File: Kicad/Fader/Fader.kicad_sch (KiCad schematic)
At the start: 8 parts, among them J1 NCJ6FA-H, J2 NCJ6FA-H, SW1 SW_DPDT_x2, SW2 SW_DPDT_x2, SW3 SW_DPST_x2, SW4 SW_DPST_x2, SW5 SW_DPDT_x2, SW6 SW_DPDT_x2

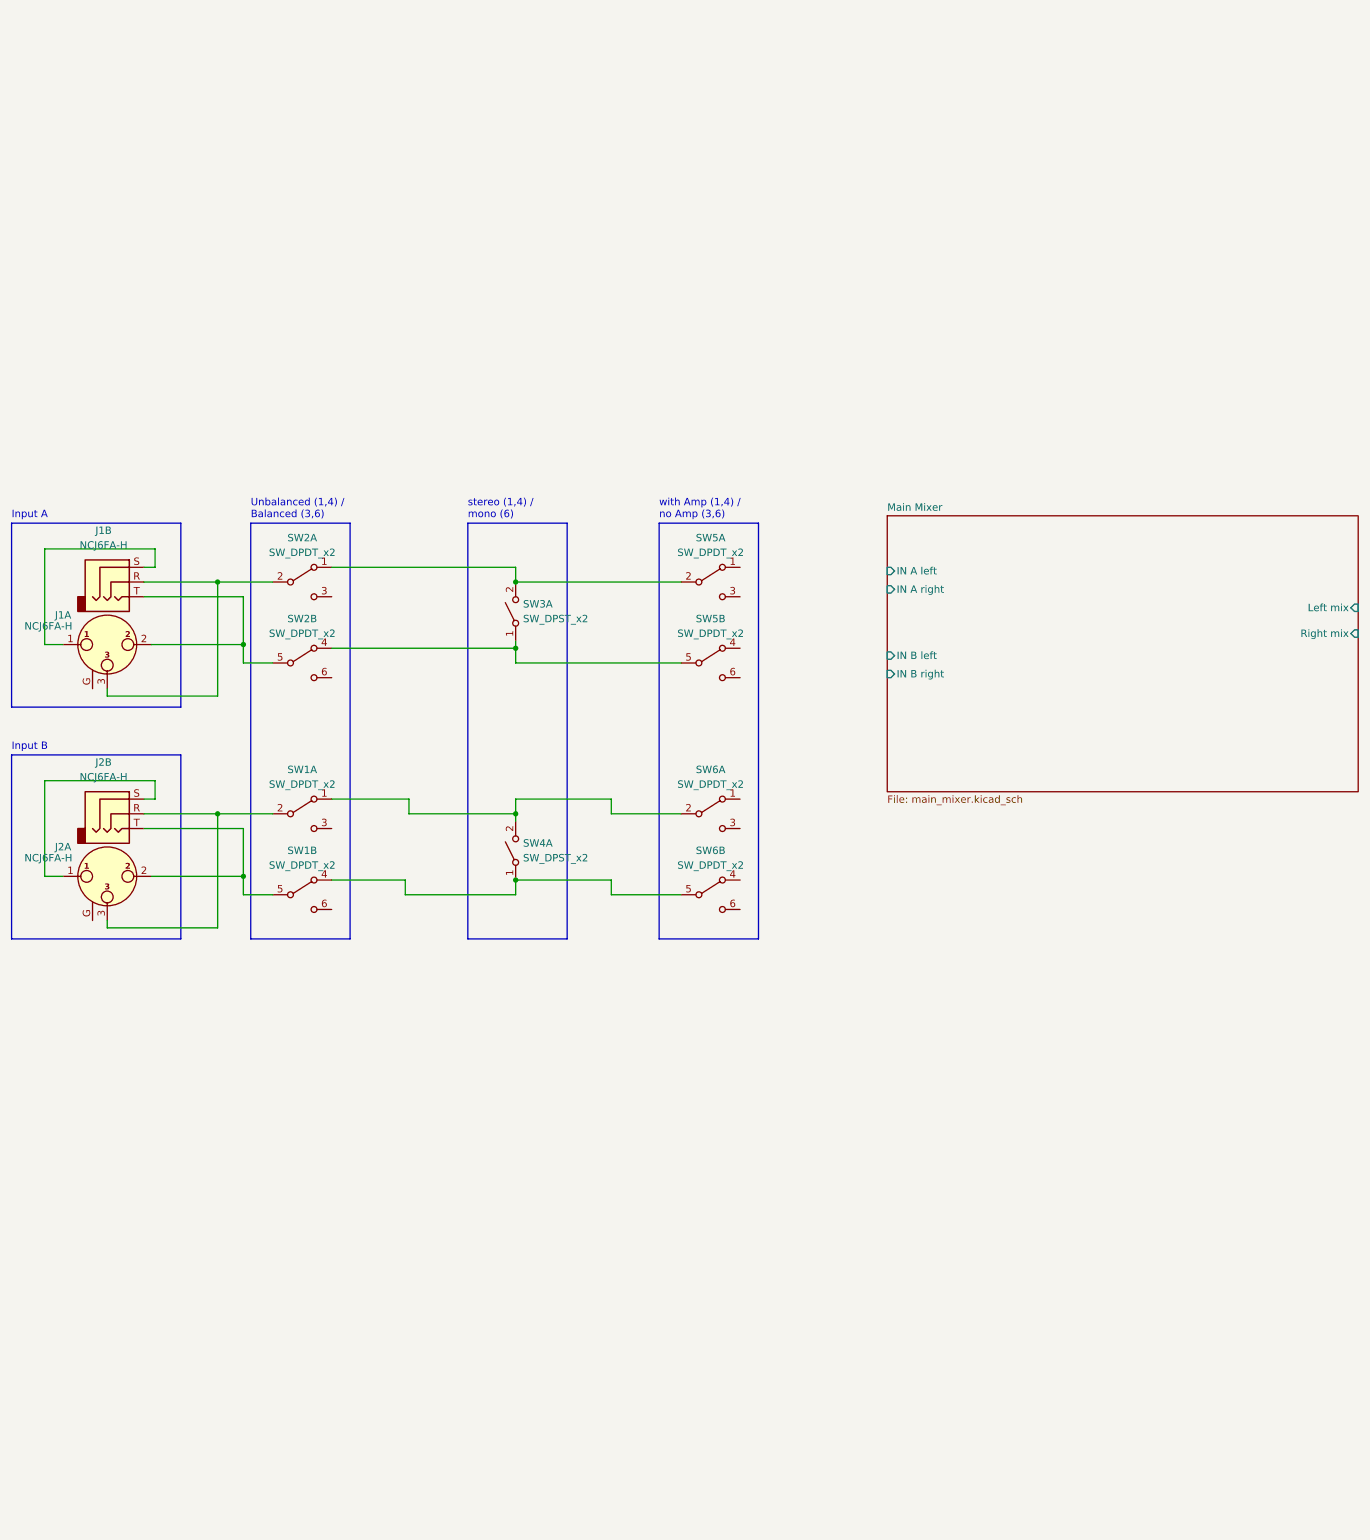
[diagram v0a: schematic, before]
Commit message: added amp and power bypass
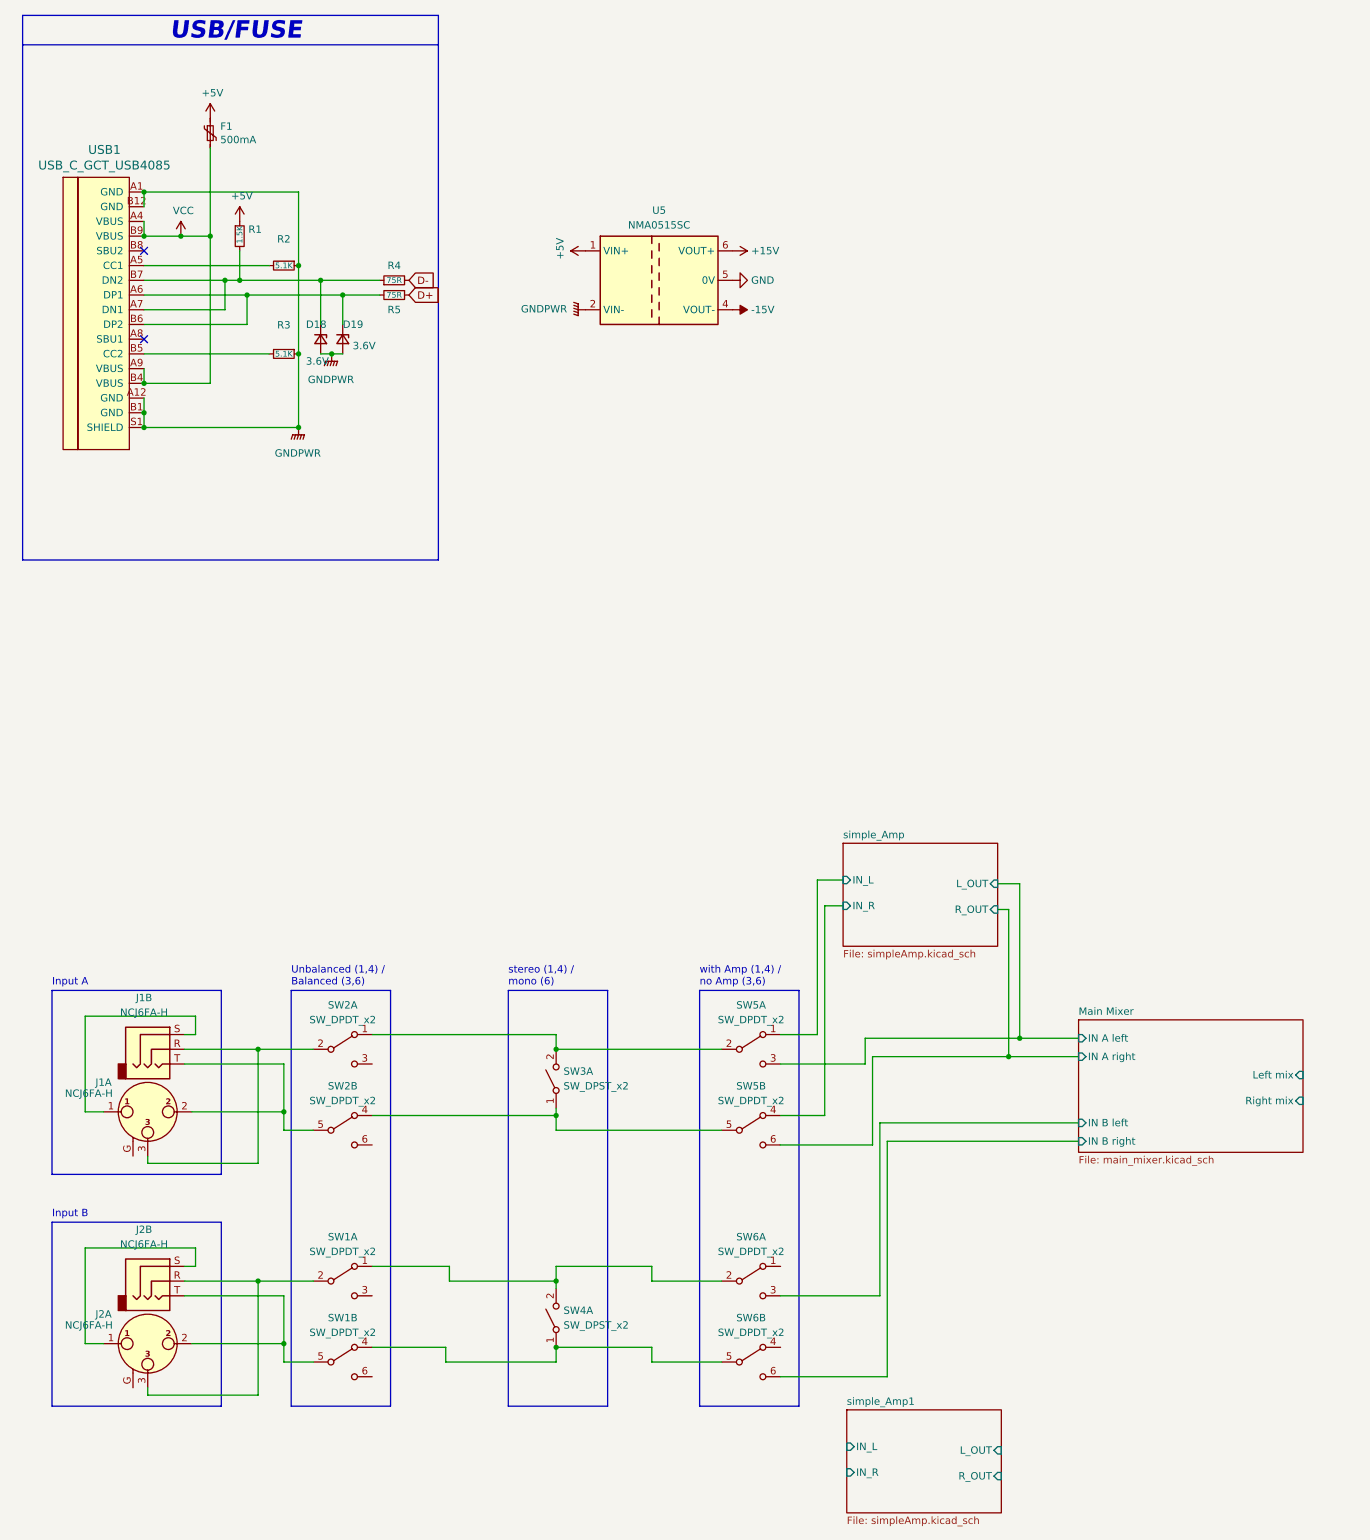
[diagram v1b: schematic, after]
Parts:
- added D18, D19: 3.6V, Diode_THT:D_DO-35_SOD27_P5.08mm_Horizontal, symbol Device:D_Zener_Small
- added F1: 500mA, keyboard_parts:polyfuse_5.1mm, symbol Device:Polyfuse_Small
- added R1: 1.5K, Resistor_THT:R_Axial_DIN0204_L3.6mm_D1.6mm_P5.08mm_Horizontal, symbol Device:R_Small
- added R2, R3: 5.1K, Resistor_THT:R_Axial_DIN0204_L3.6mm_D1.6mm_P5.08mm_Horizontal, symbol Device:R_Small
- added R4, R5: 75R, Resistor_THT:R_Axial_DIN0204_L3.6mm_D1.6mm_P5.08mm_Horizontal, symbol Device:R_Small
- added U5: NMA0515SC, Converter_DCDC:Converter_DCDC_Murata_NMAxxxxSC_THT, symbol Regulator_Switching:NMA0515SC
- added USB1: USB_C_GCT_USB4085, Type-C:USB_C_GCT_USB4085, symbol Type-C:USB_C_GCT_USB4085
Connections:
- net Main Mixer/IN A left: now also SW5.3 (C)
- net Main Mixer/IN A right: now also SW5.6 (C)
- net Main Mixer/IN B left: now also SW6.3 (C)
- net Main Mixer/IN B right: now also SW6.6 (C)
- net simple_Amp/IN_L: now reaches SW5.1 (A)
- net simple_Amp/IN_R: now reaches SW5.4 (A)
- new net: R2.2, USB1.A5 (CC1)
- new net: D19.1 (K), R5.2, USB1.A6 (DP1), USB1.B6 (DP2)
- new net: D18.1 (K), R1.2, R4.1, USB1.A7 (DN1), USB1.B7 (DN2)
- new net: R3.2, USB1.B5 (CC2)
- new net +15V: U5.6 (VOUT+)
- new net +5V: F1.1, R1.1, U5.1 (VIN+)
- new net -15V: U5.4 (VOUT-)
- new net D+: R5.1
- new net D-: R4.2
- new net GND: U5.5 (0V)
- new net GNDPWR: D18.2 (A), D19.2 (A), R2.1, R3.1, U5.2 (VIN-), USB1.A1 (GND), USB1.A12 (GND), USB1.B1 (GND), USB1.B12 (GND), USB1.S1 (SHIELD)
- new net VCC: F1.2, USB1.A4 (VBUS), USB1.A9 (VBUS), USB1.B4 (VBUS), USB1.B9 (VBUS)
- no-connect marks 0 -> 2
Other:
- added sheet simple_Amp (simpleAmp.kicad_sch)
- added sheet simple_Amp1 (simpleAmp.kicad_sch)
- note added: "USB/FUSE"
- moved on the sheet: J1A, J1B, J2A, J2B, SW1A, SW1B, SW2A, SW2B, SW3A, SW4A, SW5A, SW5B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
